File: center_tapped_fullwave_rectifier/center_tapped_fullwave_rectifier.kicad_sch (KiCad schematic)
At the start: 5 parts, among them J1 Screw_Terminal_01x03, J2 Screw_Terminal_01x02

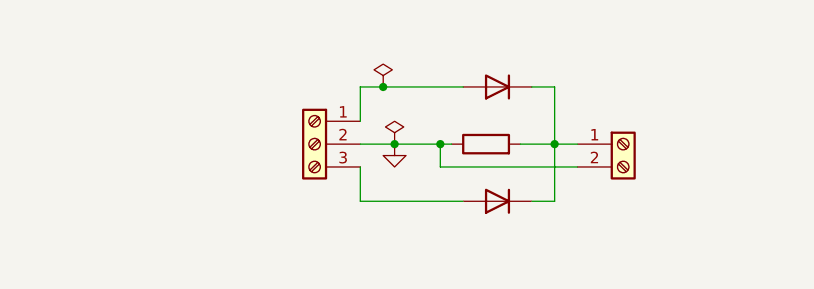
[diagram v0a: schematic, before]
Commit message: Correct Footprint of transformer and reduced hole size
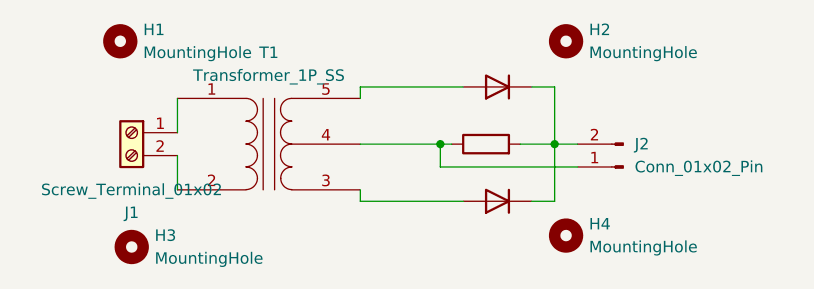
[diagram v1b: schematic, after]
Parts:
- removed J1: Screw_Terminal_01x03, TerminalBlock_Phoenix:TerminalBlock_Phoenix_MKDS-1,5-3_1x03_P5.00mm_Horizontal, symbol Connector:Screw_Terminal_01x03
- removed J2: Screw_Terminal_01x02, TerminalBlock_Phoenix:TerminalBlock_Phoenix_MKDS-1,5-2_1x02_P5.00mm_Horizontal, symbol Connector:Screw_Terminal_01x02
- added H1, H2, H3, H4: MountingHole, MountingHole:MountingHole_2.1mm, symbol Mechanical:MountingHole
- added J1: Screw_Terminal_01x02, TerminalBlock_Phoenix:TerminalBlock_Phoenix_MKDS-1,5-2-5.08_1x02_P5.08mm_Horizontal, symbol Connector:Screw_Terminal_01x02
- added J2: Conn_01x02_Pin, Connector_PinHeader_1.27mm:PinHeader_1x02_P1.27mm_Vertical_SMD_Pin1Right, symbol Connector:Conn_01x02_Pin
- added T1: Transformer_1P_SS, Transformer_SMD:Transformer_MACOM_SM-22, symbol Device:Transformer_1P_SS
- D1, D2: footprint Diode_THT:D_DO-41_SOD81_P10.16mm_Horizontal -> Diode_SMD:D_0805_2012Metric
- R1: footprint Resistor_THT:R_Axial_DIN0207_L6.3mm_D2.5mm_P10.16mm_Horizontal -> Resistor_SMD:R_0603_1608Metric
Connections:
- net at D1.2 (A): now also T1.5 (SB)
- net at D2.2 (A): now also T1.3 (SA)
- net at D1.1 (K), D2.1 (K), R1.2: now also J2.2 (Pin_2)
- net GND: no longer names the net of R1.1
- net GND: now also J2.1 (Pin_1), T1.4 (SC)
- new net: J1.1 (Pin_1), T1.1 (AA)
- new net: J1.2 (Pin_2), T1.2 (AB)
